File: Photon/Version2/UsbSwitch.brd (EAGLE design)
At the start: 52.7 x 38.1 mm, 23 parts, among them IC1 PHOTON, IC2 LM3526M-L, X1 USB A Socket, X2 USB A Socket

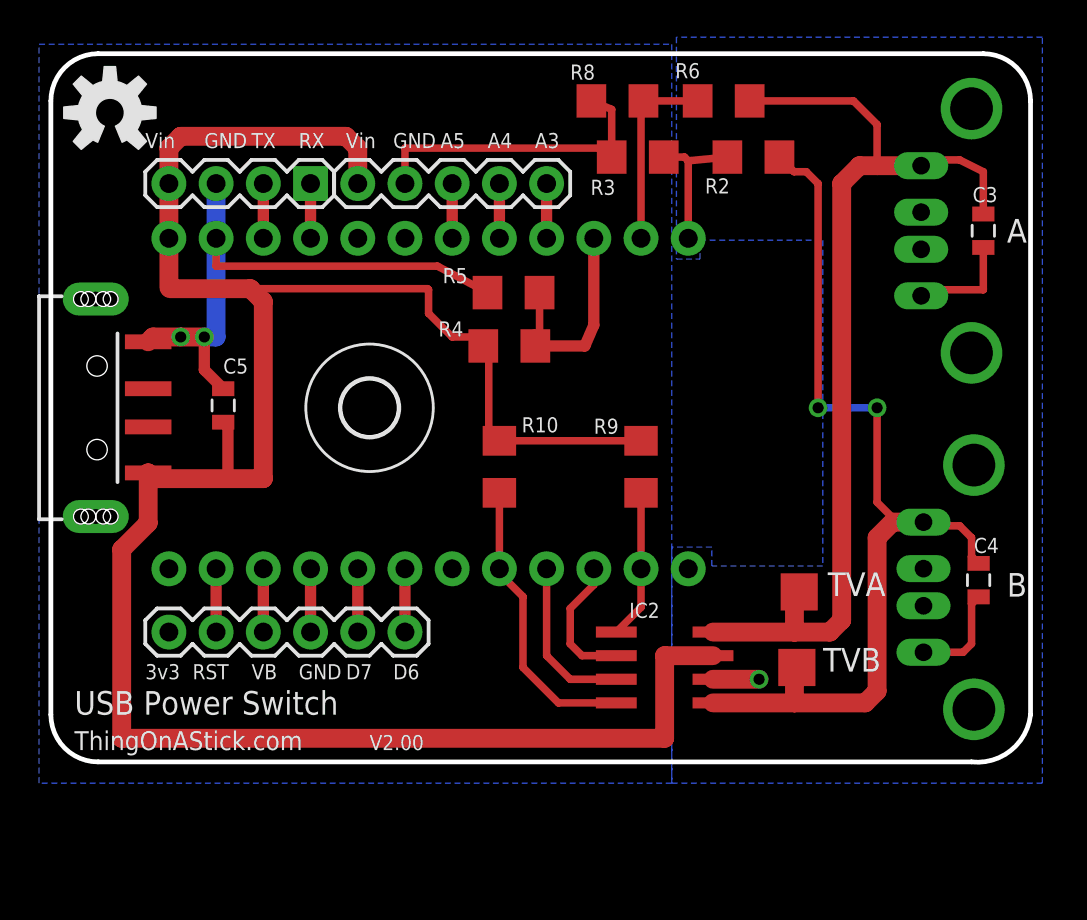
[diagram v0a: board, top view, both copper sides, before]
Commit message: Moved USB connector to top bottom side of PCB so that the Photon sticks out from the wall when put in a wall plug and that the USB in/out is not flipped.
Moved USB controller chip inside the photon and put connectors for the photon pins all along appropriate pins.
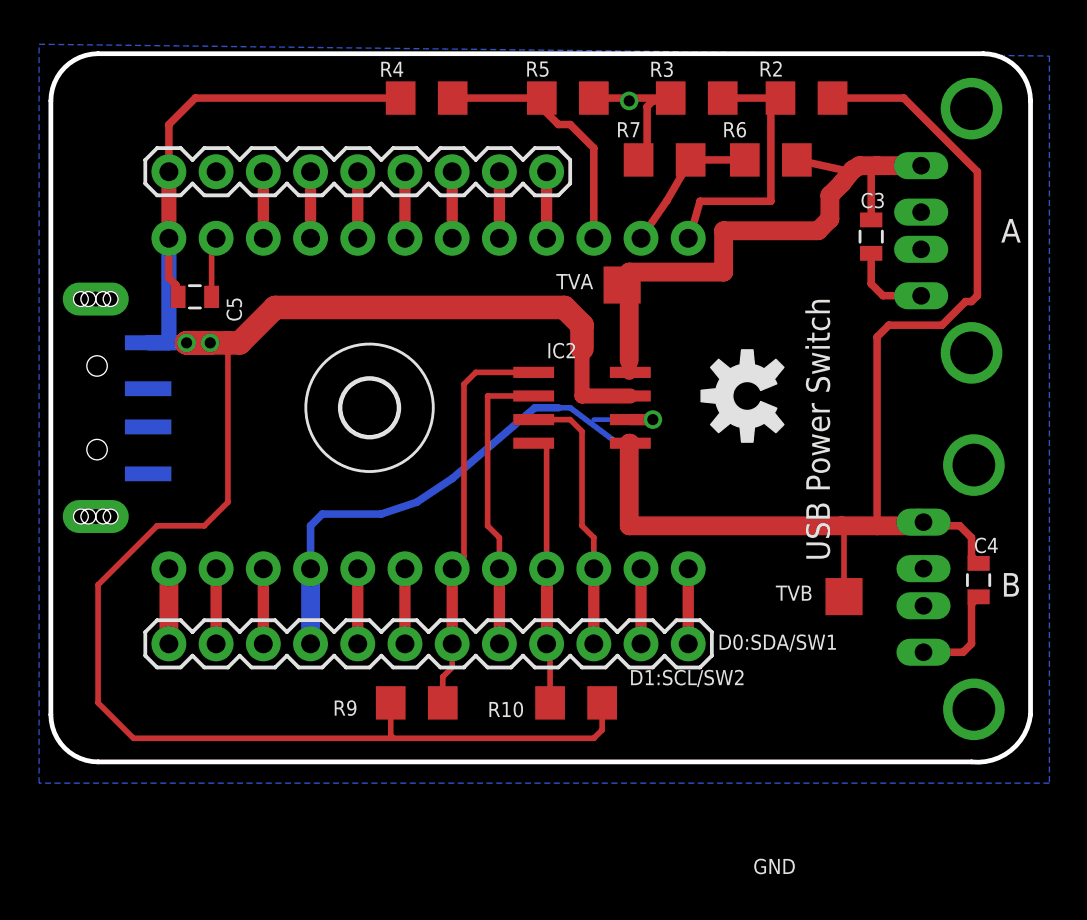
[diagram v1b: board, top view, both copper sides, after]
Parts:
- removed JP2: (no value), SparkFun-Connectors:1X04
- removed JP4: (no value), SparkFun-Connectors:1X06
- removed R8: 10k, SparkFun-Passives:1206
- added CN1: USBA-SMD-MALE, SparkFun-Connectors:USB-A-SMT-MALE
- added FRAME2: FRAME-LETTER, SparkFun-Aesthetics:CREATIVE_COMMONS
- added R7: 10k, SparkFun-Passives:1206
- JP1: value USBA-SMD-MALE -> (none); device SparkFun-Connectors:USB-A-SMT-MALE -> SparkFun-Connectors:1X12
- JP3: device SparkFun-Connectors:1X05 -> SparkFun-Connectors:1X09
- moved LOGO2 37.5 mm to (38.1, 86.4), turned to 90 degrees
- moved TVA 19.1 mm to (31.4, 92.3)
- moved R9 17.5 mm to (20.3, 69.8), turned to 180 degrees
- moved IC2 14.7 mm to (29.2, 85.7)
- moved JP1 14.5 mm to (6.99, 73.0), turned to 0 degrees
- moved R4 14.1 mm to (20.9, 102.4)
- moved R10 13.4 mm to (28.9, 69.8), turned to 0 degrees
- moved R5 10.9 mm to (28.4, 102.4), turned to 180 degrees
- moved C3 6.04 mm to (44.8, 94.9)
- moved C5 6.04 mm to (8.38, 91.7), turned to 180 degrees
- moved TVB 4.58 mm to (43.3, 75.6)
- moved R3 4.49 mm to (35.4, 102.4)
- moved R2 4.27 mm to (41.3, 102.4)
- moved R6 4.07 mm to (39.4, 99.1)
- moved JP3 0.63 mm to (27.3, 98.4)
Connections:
- removed net SWITCH1: IC1.18
- removed net SWITCH2: IC1.13
- new net N$1: IC1.6, JP3.4
- new net N$16: IC1.3, JP3.7
- new net SCL/SWITCH2: IC1.14, JP1.11
- new net SDA/SWITCH1: IC1.13, JP1.12
- net 3.3V: now also JP1.1; no longer JP4.1
- net GND: now also CN1.GND1, JP1.4, JP3.8, R7.1; no longer JP1.GND1, JP2.3, JP3.4, JP4.4, R8.1
- net N$12: now also JP1.6; no longer JP4.6
- net N$13: now also JP1.5; no longer JP4.5
- net N$14: now also JP1.3; no longer JP4.3
- net N$15: now also JP1.2; no longer JP4.2
- net N$3: now also IC1.5, JP3.5; no longer IC1.3, JP2.2
- net N$4: now also JP3.6; no longer JP2.1
- net N$5: now also R7.2; no longer R8.2
- net USBFLAGA: now also IC1.17, JP1.8; no longer IC1.15
- net USBFLAGB: now also IC1.15, JP1.10; no longer IC1.16
- net USBVPOWERENABLEA: now also IC1.18, JP1.7; no longer IC1.14
- net USBVPOWERENABLEB: now also IC1.16, JP1.9; no longer IC1.17
- net VIN: now also CN1.VBUS1, JP3.9; no longer JP1.VBUS1, JP2.4, JP3.5
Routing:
- net VUSBOUTA: track 53.1 -> 32.7 mm
- net USBVPOWERENABLEA: track 8.04 -> 21.6 mm
- net VUSBOUTB: track 51.2 -> 61.8 mm, vias 2 -> 0
- net GND: track 65.7 -> 55.5 mm, vias 3 -> 2
- net USBFLAGA: track 7.31 -> 16.1 mm
- net N$21: track 7.68 -> 15.2 mm
- net USBFLAGB: track 8.95 -> 14.6 mm
- net VIN: track 123.2 -> 118.0 mm, vias 0 -> 2
- net SDA/SWITCH1: track 0.00 -> 4.04 mm
- net SCL/SWITCH2: track 0.00 -> 4.04 mm
- net 3.3V: track 0.00 -> 4.04 mm
- net N$16: track 0.00 -> 3.58 mm
- net N$1: track 0.00 -> 3.58 mm
- net USBVPOWERENABLEB: track 15.7 -> 18.8 mm
- net N$5: track 10.7 -> 7.91 mm
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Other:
- board text added: "5V"
- board text added: "A0"
- board text added: "A1"
- board text added: "A2"
- board text added: "D0"
- board text added: "D0:SDA/SW1"
- board text added: "D1"
- board text added: "D1:SCL/SW2"
- board text added: "D2"
- board text added: "D3"
- board text added: "D4"
- board text added: "D5"
- board text added: "DAC"
- board text added: "ThingOnAStick.com/UsbSwitch"
- board text added: "V2.02"
- board text added: "WKP"
- board text removed: "All Through Hole Parts mounted on PBC Bottom layer."
- board text removed: "ThingOnAStick.com"
- board text removed: "V2.00"
- board text removed: "Vin"
